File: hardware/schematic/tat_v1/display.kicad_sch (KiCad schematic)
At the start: 17 parts, among them J4 24-pin FPC 0.5mm, Top Contact, Q1 Q_NMOS

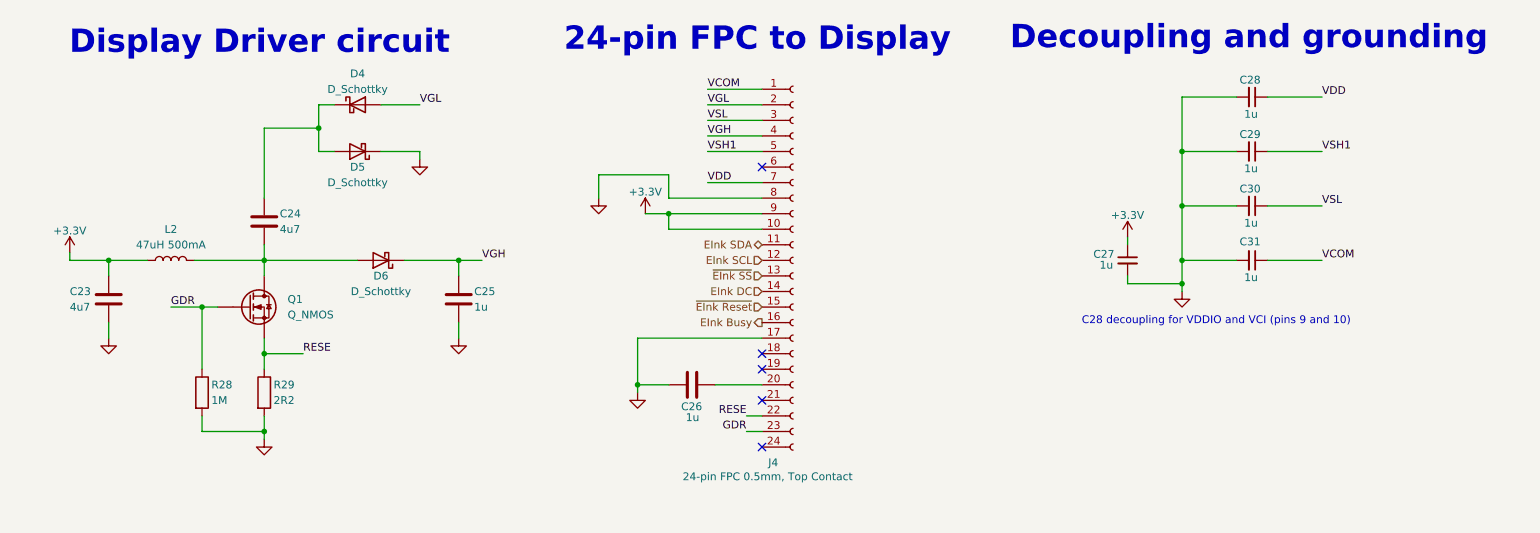
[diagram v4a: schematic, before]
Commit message: Most simple footprints added. Need to create footprints for more complex parts.
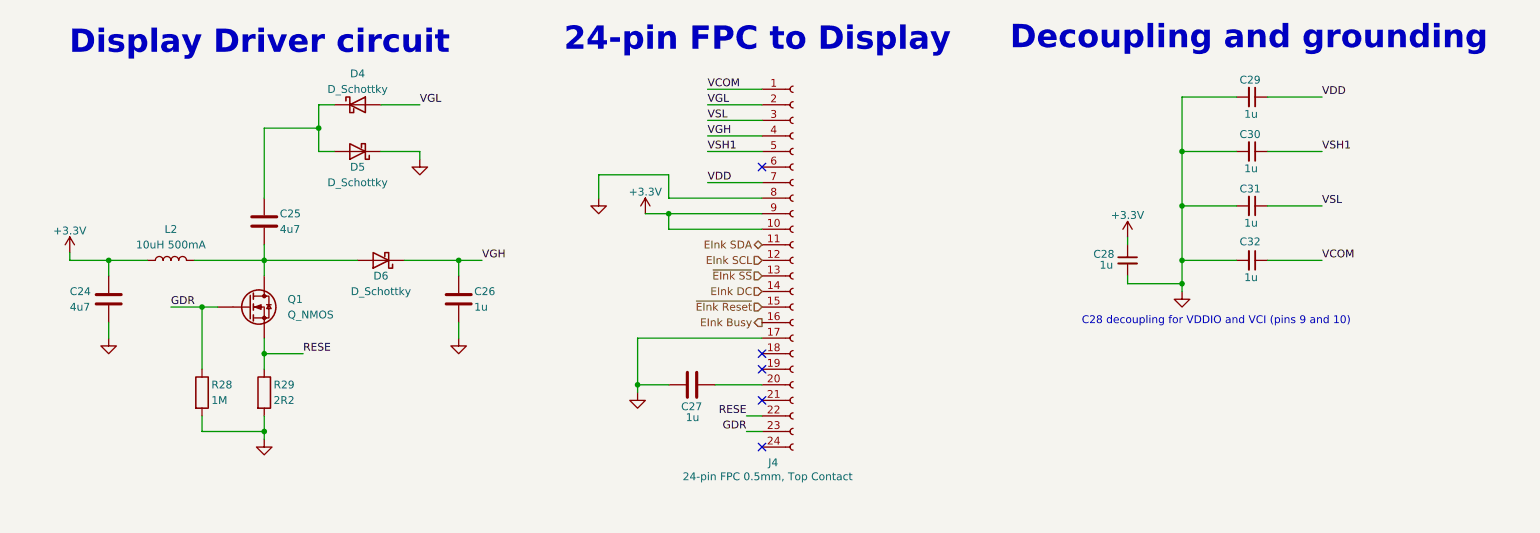
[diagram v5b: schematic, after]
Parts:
- C24: renamed from C23; footprint (none) -> Capacitor_SMD:C_0603_1608Metric; Link (none) -> https://www.lcsc.com/product-detail/Multilayer-Ceramic-Capa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
- C25: renamed from C24; footprint (none) -> Capacitor_SMD:C_0603_1608Metric; Link (none) -> https://www.lcsc.com/product-detail/Multilayer-Ceramic-Capa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
- C26: renamed from C25; footprint (none) -> Capacitor_SMD:C_0603_1608Metric; Link (none) -> https://www.lcsc.com/product-detail/Multilayer-Ceramic-Capa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
- C27: renamed from C26; footprint (none) -> Capacitor_SMD:C_0603_1608Metric; Link (none) -> https://www.lcsc.com/product-detail/Multilayer-Ceramic-Capa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
- C28: renamed from C27; footprint (none) -> Capacitor_SMD:C_0603_1608Metric; Link (none) -> https://www.lcsc.com/product-detail/Multilayer-Ceramic-Capa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
- C29: renamed from C28; footprint (none) -> Capacitor_SMD:C_0603_1608Metric; Link (none) -> https://www.lcsc.com/product-detail/Multilayer-Ceramic-Capa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
- C30: renamed from C29; footprint (none) -> Capacitor_SMD:C_0603_1608Metric; Link (none) -> https://www.lcsc.com/product-detail/Multilayer-Ceramic-Capa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
- C31: renamed from C30; footprint (none) -> Capacitor_SMD:C_0603_1608Metric; Link (none) -> https://www.lcsc.com/product-detail/Multilayer-Ceramic-Capa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
- C32: renamed from C31; footprint (none) -> Capacitor_SMD:C_0603_1608Metric; Link (none) -> https://www.lcsc.com/product-detail/Multilayer-Ceramic-Capa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
- D4, D5, D6: footprint (none) -> Diode_SMD:D_SOD-123; Link (none) -> https://www.lcsc.com/product-detail/Schottky-Diodes_Jiangsu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
- L2: value 47uH 500mA -> 10uH 500mA; footprint (none) -> Inductor_SMD:L_0805_2012Metric; Link (none) -> https://www.lcsc.com/product-detail/Inductors-SMD_microgate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
- Q1: Link (none) -> https://www.lcsc.com/product-detail/MOSFETs_Alpha-Omega-Sem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
- R28, R29: footprint (none) -> Resistor_SMD:R_0603_1608Metric; Link (none) -> https://www.lcsc.com/product-detail/Chip-Resistor-Surface-M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

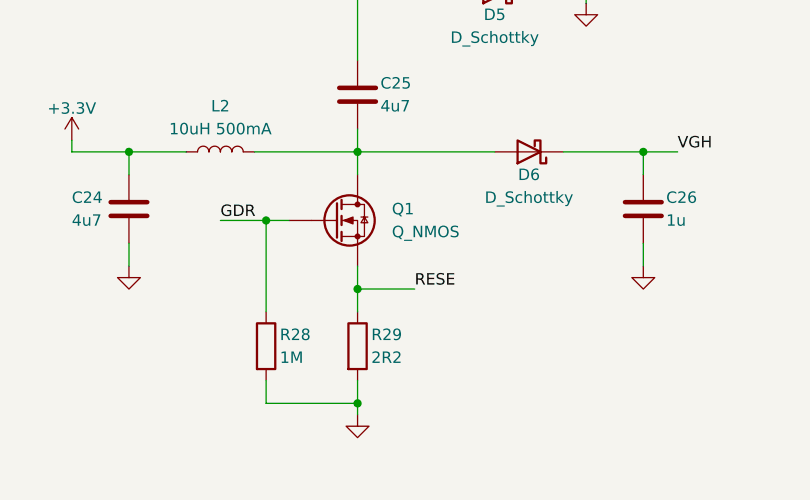
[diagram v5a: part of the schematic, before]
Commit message: Finished all footprints, can now start laying out circuit
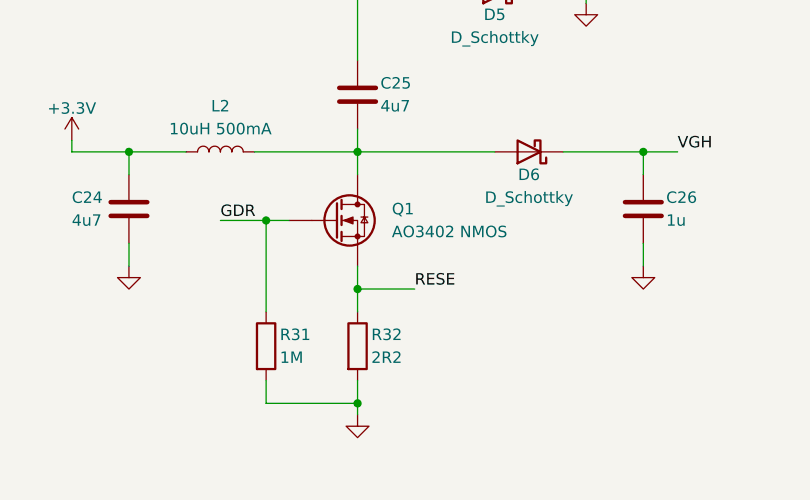
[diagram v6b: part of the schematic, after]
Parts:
- J4: footprint (none) -> Connector_FFC-FPC:Jushuo_AFC07-S24FCA-00_1x24-1MP_P0.50_Horizontal; Link (none) -> https://www.lcsc.com/product-detail/FFC-FPC-Flat-Flexible-C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
- Q1: value Q_NMOS -> AO3402 NMOS; footprint (none) -> Package_TO_SOT_SMD:SOT-23
- renumbered R28 to R31, R29 to R32
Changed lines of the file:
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@@
 			)
 		)
-		(property "Footprint" ""
+		(property "Footprint" "Connector_FFC-FPC:Jushuo_AFC07-S24FCA-00_1x24-1MP_P0.50_Horizontal"
 			(at 154.94 99.06 0)
 			(effects
@@
 			)
 		)
-		(property "Datasheet" "~"
+		(property "Datasheet" "https://www.lcsc.com/datasheet/lcsc_datasheet_2504101957_JUSHUO-AFC07-S24ECA-00_C262643.pdf"
 			(at 154.94 99.06 0)
 			(effects
@@
 			)
 		)
-		(property "Description" "Generic connector, single row, 01x24, script generated"
+		(property "Description" "24-socket FPC, 0.5mm pitch, slide lock"
+			(at 154.94 99.06 0)
+			(effects
+				(font
+					(size 1.27 1.27)
+				)
+				(hide yes)
+			)
+		)
+		(property "Link" "https://www.lcsc.com/product-detail/FFC-FPC-Flat-Flexible-Connector-Assemblies_JUSHUO-AFC07-S24ECA-00_C262643.html?s_z=n_JUSHUO%2520AFC07-S24ECA-00"
 			(at 154.94 99.06 0)
 			(effects
@@
 		(on_board yes)
 		(dnp no)
-		(property "Reference" "R28"
+		(property "Reference" "R31"
 			(at 59.944 119.38 0)
 			(effects
@@
 			(project "tat_v1"
 				(path "/b6d2ddf1-6792-45dd-afc9-29fd74d587ec/3e709284-5543-4534-bf58-110f53ad5a3b"
-					(reference "R28")
+					(reference "R31")
 					(unit 1)
 				)
@@
 			)
 		)
-		(property "Value" "Q_NMOS"
+		(property "Value" "AO3402 NMOS"
 			(at 72.39 107.9499 0)
 			(effects
@@
 			)
 		)
-		(property "Footprint" ""
+		(property "Footprint" "Package_TO_SOT_SMD:SOT-23"
 			(at 71.12 104.14 0)
 			(effects
@@
 		(on_board yes)
 		(dnp no)
-		(property "Reference" "R29"
+		(property "Reference" "R32"
 			(at 70.104 119.38 0)
 			(effects
@@
 			(project ""
 				(path "/b6d2ddf1-6792-45dd-afc9-29fd74d587ec/3e709284-5543-4534-bf58-110f53ad5a3b"
-					(reference "R29")
-					(unit 1)
-				)
+					(reference "R32")
+					(unit 1)
+				)

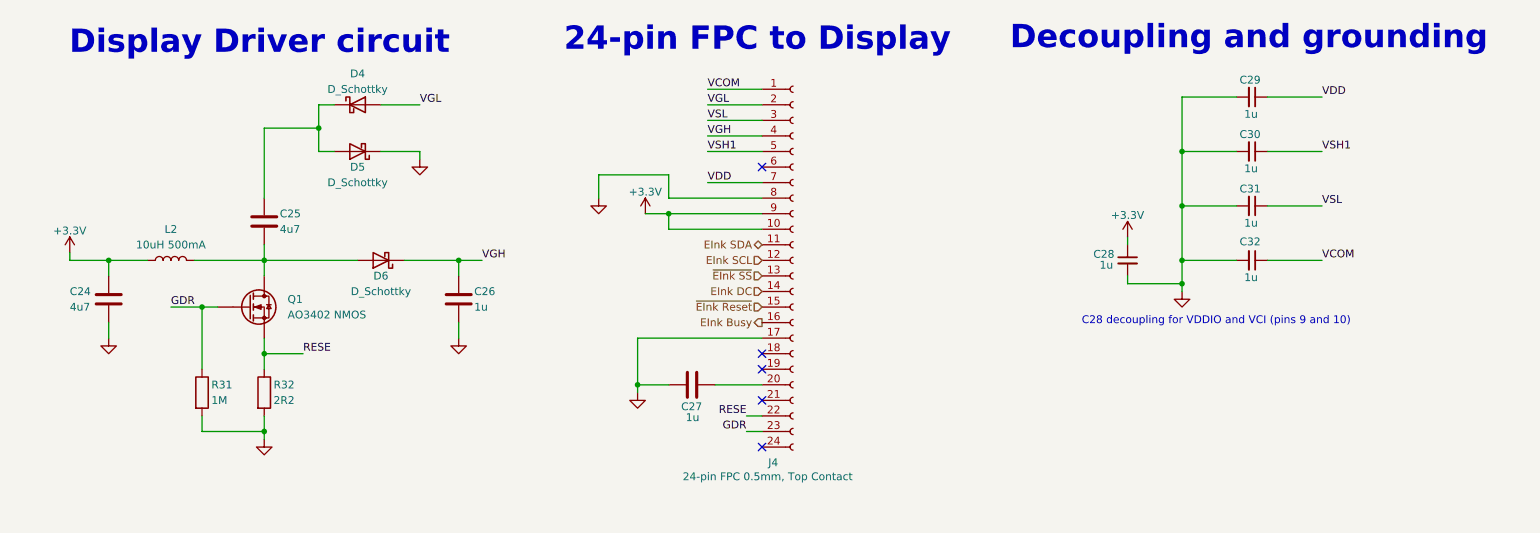
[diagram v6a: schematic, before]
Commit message: Fixed all footprint-symbol mismatches, ready to start routing!
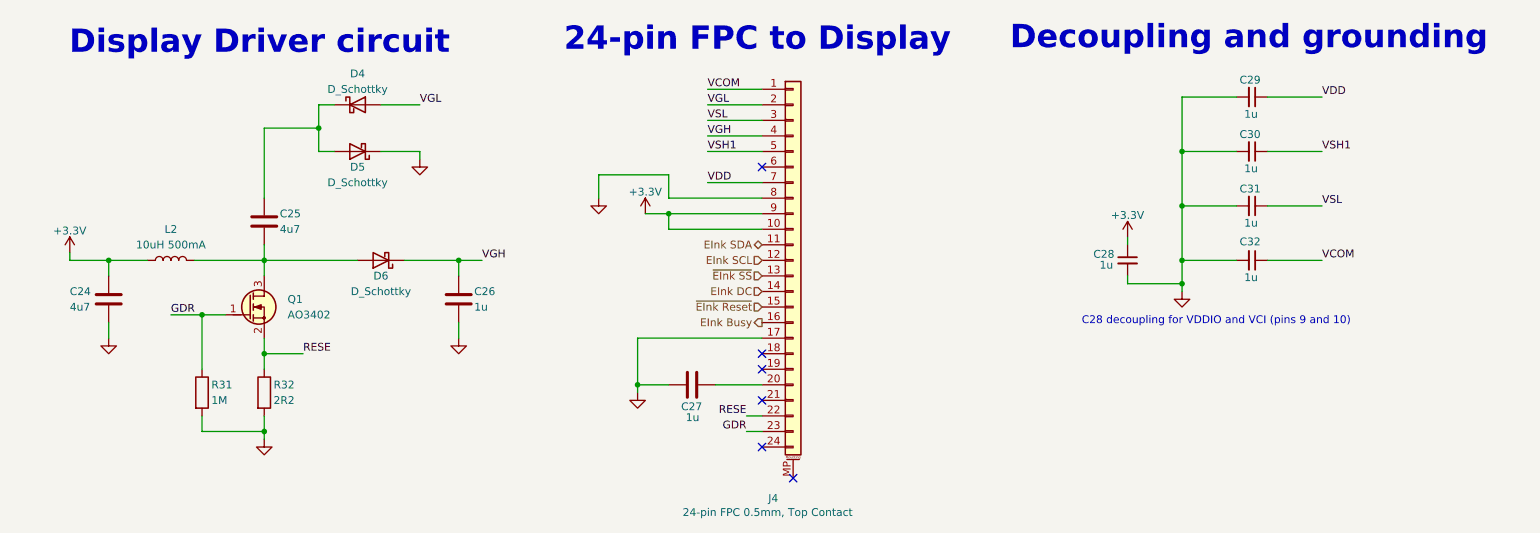
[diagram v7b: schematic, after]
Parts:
- removed Q1: AO3402 NMOS, Package_TO_SOT_SMD:SOT-23, symbol Device:Q_NMOS
- added Q1: AO3402, PCM_Package_TO_SOT_SMD_AKL:SOT-23, symbol PCM_Transistor_MOSFET_AKL:AO3402
- J4: symbol Connector:Conn_01x24_Socket -> Connector_Generic_MountingPin:Conn_01x24_MountingPin
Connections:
- net GDR: now also Q1.1 (G)
- net RESE: now also Q1.2 (S)
- net at C25.2, D6.2 (A), L2.2: now also Q1.3 (D)
- no-connect marks 5 -> 6
